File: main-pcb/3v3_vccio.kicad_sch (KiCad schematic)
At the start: 1 part, among them U1 XC7S100-1FGGA484C

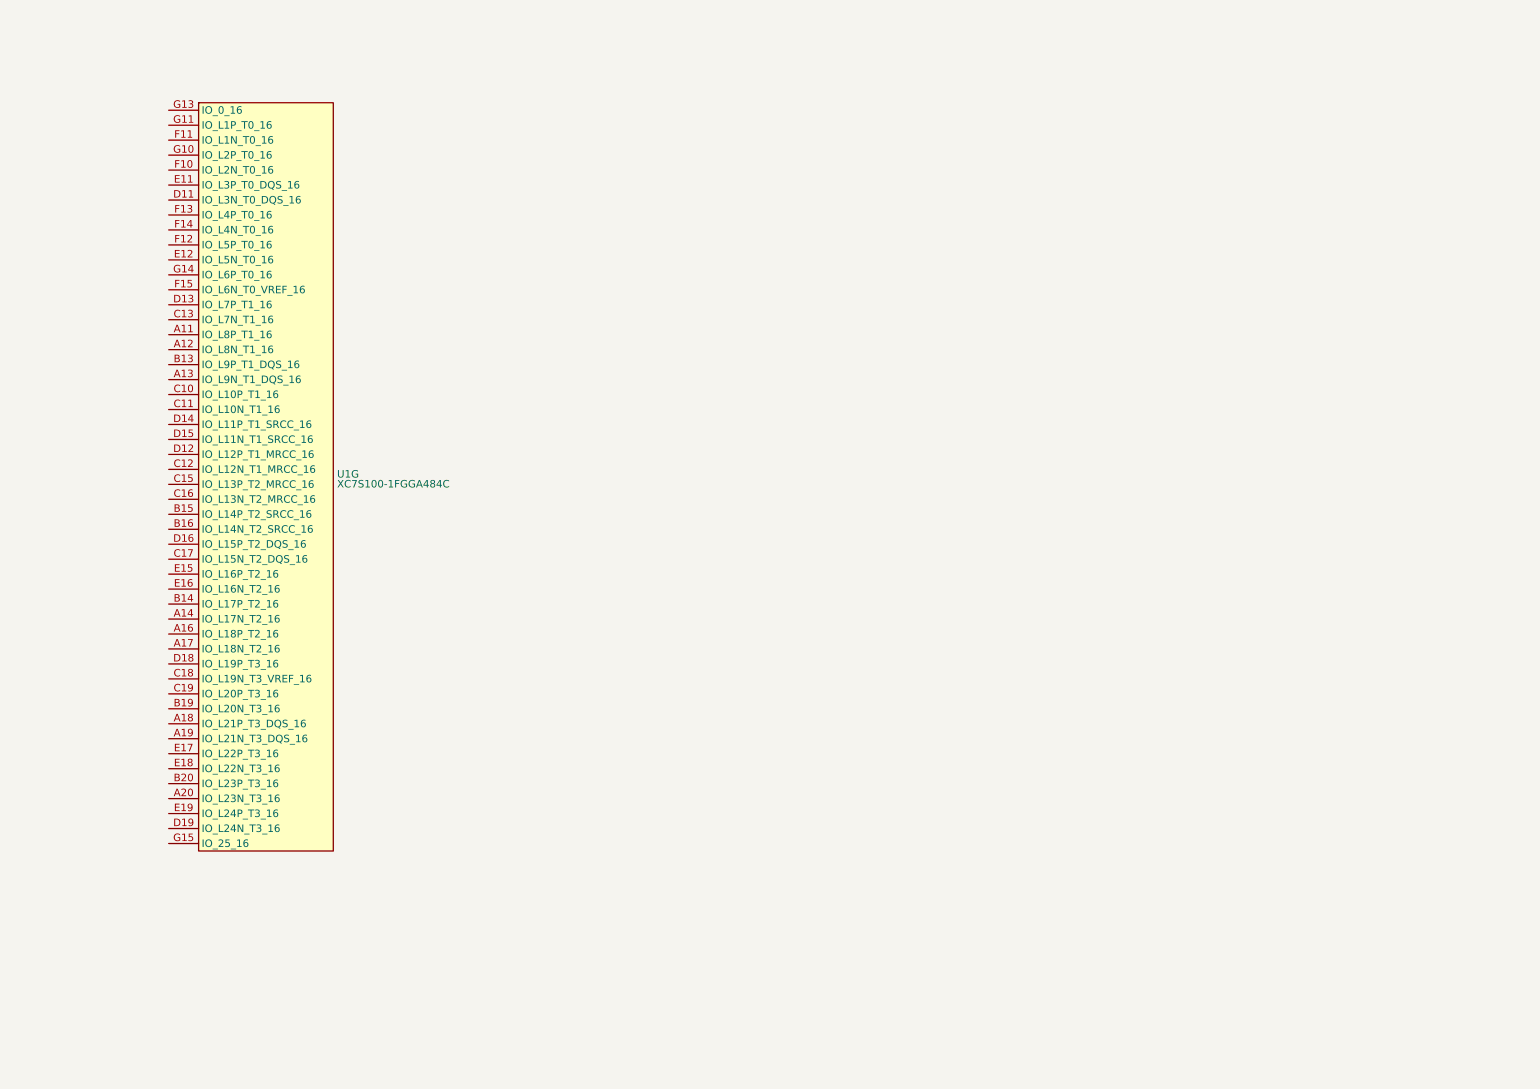
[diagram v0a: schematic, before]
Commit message: Initial design mostly done aside from USB connector, review, test points
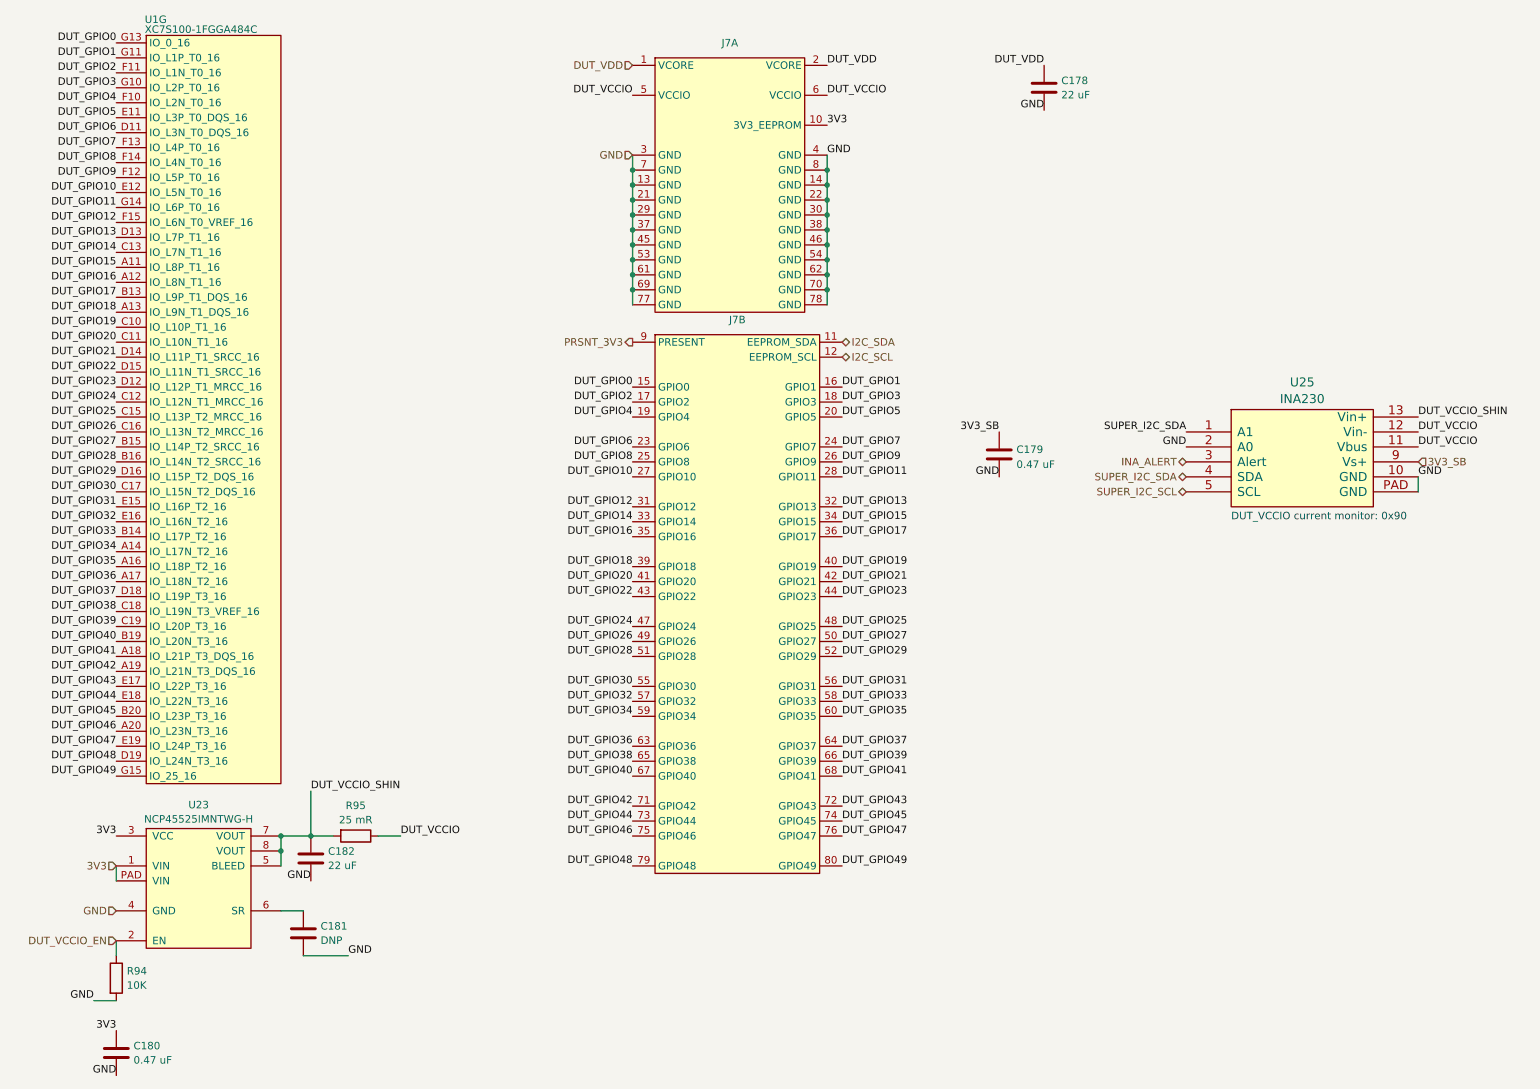
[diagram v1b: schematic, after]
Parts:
- added C178, C182: 22 uF, symbol device:C
- added C179: 0.47 uF, azonenberg_pcb:EIA_0402_CAP_NOSILK, symbol device:C
- added C180: 0.47 uF, symbol device:C
- added C181: DNP, symbol device:C
- added J7: ~, symbol special-azonenberg:CONN_DUMPTRUCK_HOST
- added R94: 10K, symbol device:R
- added R95: 25 mR, symbol passive-azonenberg:R_PWR
- added U23: NCP45525IMNTWG-H, symbol power-azonenberg:NCP45525
- added U25: INA230, azonenberg_pcb:QFN_16_0.5MM_3x3MM, symbol special-azonenberg:INA230
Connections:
- net DUT_GPIO15: now reaches U1.A11 (IO_L8P_T1_16)
- net DUT_GPIO15: now also J7.34 (GPIO15)
- net DUT_GPIO16: now reaches U1.A12 (IO_L8N_T1_16)
- net DUT_GPIO16: now also J7.35 (GPIO16)
- net DUT_GPIO18: now reaches U1.A13 (IO_L9N_T1_DQS_16)
- net DUT_GPIO18: now also J7.39 (GPIO18)
- net DUT_GPIO34: now reaches U1.A14 (IO_L17N_T2_16)
- net DUT_GPIO34: now also J7.59 (GPIO34)
- net DUT_GPIO35: now reaches U1.A16 (IO_L18P_T2_16)
- net DUT_GPIO35: now also J7.60 (GPIO35)
- net DUT_GPIO36: now reaches U1.A17 (IO_L18N_T2_16)
- net DUT_GPIO36: now also J7.63 (GPIO36)
- net DUT_GPIO41: now reaches U1.A18 (IO_L21P_T3_DQS_16)
- net DUT_GPIO41: now also J7.68 (GPIO41)
- net DUT_GPIO42: now reaches U1.A19 (IO_L21N_T3_DQS_16)
- net DUT_GPIO42: now also J7.71 (GPIO42)
- net DUT_GPIO46: now reaches U1.A20 (IO_L23N_T3_16)
- net DUT_GPIO46: now also J7.75 (GPIO46)
- net DUT_GPIO17: now reaches U1.B13 (IO_L9P_T1_DQS_16)
- net DUT_GPIO17: now also J7.36 (GPIO17)
- net DUT_GPIO33: now reaches U1.B14 (IO_L17P_T2_16)
- net DUT_GPIO33: now also J7.58 (GPIO33)
- net DUT_GPIO27: now reaches U1.B15 (IO_L14P_T2_SRCC_16)
- net DUT_GPIO27: now also J7.50 (GPIO27)
- net DUT_GPIO28: now reaches U1.B16 (IO_L14N_T2_SRCC_16)
- net DUT_GPIO28: now also J7.51 (GPIO28)
- net DUT_GPIO40: now reaches U1.B19 (IO_L20N_T3_16)
- net DUT_GPIO40: now also J7.67 (GPIO40)
- net DUT_GPIO45: now reaches U1.B20 (IO_L23P_T3_16)
- net DUT_GPIO45: now also J7.74 (GPIO45)
- net DUT_GPIO19: now reaches U1.C10 (IO_L10P_T1_16)
- net DUT_GPIO19: now also J7.40 (GPIO19)
- net DUT_GPIO20: now reaches U1.C11 (IO_L10N_T1_16)
- net DUT_GPIO20: now also J7.41 (GPIO20)
- net DUT_GPIO24: now reaches U1.C12 (IO_L12N_T1_MRCC_16)
- net DUT_GPIO24: now also J7.47 (GPIO24)
- net DUT_GPIO14: now reaches U1.C13 (IO_L7N_T1_16)
- net DUT_GPIO14: now also J7.33 (GPIO14)
- net DUT_GPIO25: now reaches U1.C15 (IO_L13P_T2_MRCC_16)
- net DUT_GPIO25: now also J7.48 (GPIO25)
- net DUT_GPIO26: now reaches U1.C16 (IO_L13N_T2_MRCC_16)
- net DUT_GPIO26: now also J7.49 (GPIO26)
- net DUT_GPIO30: now reaches U1.C17 (IO_L15N_T2_DQS_16)
- net DUT_GPIO30: now also J7.55 (GPIO30)
- net DUT_GPIO38: now reaches U1.C18 (IO_L19N_T3_VREF_16)
- net DUT_GPIO38: now also J7.65 (GPIO38)
- net DUT_GPIO39: now reaches U1.C19 (IO_L20P_T3_16)
- net DUT_GPIO39: now also J7.66 (GPIO39)
- net DUT_GPIO6: now reaches U1.D11 (IO_L3N_T0_DQS_16)
- net DUT_GPIO6: now also J7.23 (GPIO6)
- net DUT_GPIO23: now reaches U1.D12 (IO_L12P_T1_MRCC_16)
- net DUT_GPIO23: now also J7.44 (GPIO23)
- net DUT_GPIO13: now reaches U1.D13 (IO_L7P_T1_16)
- net DUT_GPIO13: now also J7.32 (GPIO13)
- net DUT_GPIO21: now reaches U1.D14 (IO_L11P_T1_SRCC_16)
- net DUT_GPIO21: now also J7.42 (GPIO21)
- net DUT_GPIO22: now reaches U1.D15 (IO_L11N_T1_SRCC_16)
- net DUT_GPIO22: now also J7.43 (GPIO22)
- net DUT_GPIO29: now reaches U1.D16 (IO_L15P_T2_DQS_16)
- net DUT_GPIO29: now also J7.52 (GPIO29)
- net DUT_GPIO37: now reaches U1.D18 (IO_L19P_T3_16)
- net DUT_GPIO37: now also J7.64 (GPIO37)
- net DUT_GPIO48: now reaches U1.D19 (IO_L24N_T3_16)
- net DUT_GPIO48: now also J7.79 (GPIO48)
- net DUT_GPIO5: now reaches U1.E11 (IO_L3P_T0_DQS_16)
- net DUT_GPIO5: now also J7.20 (GPIO5)
- net DUT_GPIO10: now reaches U1.E12 (IO_L5N_T0_16)
- net DUT_GPIO10: now also J7.27 (GPIO10)
- net DUT_GPIO31: now reaches U1.E15 (IO_L16P_T2_16)
- net DUT_GPIO31: now also J7.56 (GPIO31)
- net DUT_GPIO32: now reaches U1.E16 (IO_L16N_T2_16)
- net DUT_GPIO32: now also J7.57 (GPIO32)
- net DUT_GPIO43: now reaches U1.E17 (IO_L22P_T3_16)
- net DUT_GPIO43: now also J7.72 (GPIO43)
- net DUT_GPIO44: now reaches U1.E18 (IO_L22N_T3_16)
- net DUT_GPIO44: now also J7.73 (GPIO44)
- net DUT_GPIO47: now reaches U1.E19 (IO_L24P_T3_16)
- net DUT_GPIO47: now also J7.76 (GPIO47)
- net DUT_GPIO4: now reaches U1.F10 (IO_L2N_T0_16)
- net DUT_GPIO4: now also J7.19 (GPIO4)
- net DUT_GPIO2: now reaches U1.F11 (IO_L1N_T0_16)
- net DUT_GPIO2: now also J7.17 (GPIO2)
- net DUT_GPIO9: now reaches U1.F12 (IO_L5P_T0_16)
- net DUT_GPIO9: now also J7.26 (GPIO9)
- net DUT_GPIO7: now reaches U1.F13 (IO_L4P_T0_16)
- net DUT_GPIO7: now also J7.24 (GPIO7)
- net DUT_GPIO8: now reaches U1.F14 (IO_L4N_T0_16)
- net DUT_GPIO8: now also J7.25 (GPIO8)
- net DUT_GPIO12: now reaches U1.F15 (IO_L6N_T0_VREF_16)
- net DUT_GPIO12: now also J7.31 (GPIO12)
- net DUT_GPIO3: now reaches U1.G10 (IO_L2P_T0_16)
- net DUT_GPIO3: now also J7.18 (GPIO3)
- net DUT_GPIO1: now reaches U1.G11 (IO_L1P_T0_16)
- net DUT_GPIO1: now also J7.16 (GPIO1)
- net DUT_GPIO0: now reaches U1.G13 (IO_0_16)
- net DUT_GPIO0: now also J7.15 (GPIO0)
- net DUT_GPIO11: now reaches U1.G14 (IO_L6P_T0_16)
- net DUT_GPIO11: now also J7.28 (GPIO11)
- net DUT_GPIO49: now reaches U1.G15 (IO_25_16)
- net DUT_GPIO49: now also J7.80 (GPIO49)
- new net: C181.1, U23.6 (SR)
- new net 3V3: C180.1, J7.10 (3V3_EEPROM), U23.1 (VIN), U23.3 (VCC), U23.PAD (VIN)
- new net 3V3_SB: C179.1, U25.9 (Vs+)
- new net DUT_VCCIO: J7.5 (VCCIO), J7.6 (VCCIO), R95.1, U25.11 (Vbus), U25.12 (Vin-)
- new net DUT_VCCIO_EN: R94.1, U23.2 (EN)
- new net DUT_VCCIO_SHIN: C182.1, R95.2, U23.5 (BLEED), U23.7 (VOUT), U23.8 (VOUT), U25.13 (Vin+)
- new net DUT_VDD: C178.1, J7.1 (VCORE), J7.2 (VCORE)
- new net GND: C178.2, C179.2, C180.2, C181.2, C182.2, J7.13 (GND), J7.14 (GND), J7.21 (GND), J7.22 (GND), J7.29 (GND), J7.3 (GND), J7.30 (GND), J7.37 (GND), J7.38 (GND), J7.4 (GND), J7.45 (GND), J7.46 (GND), J7.53 (GND), J7.54 (GND), J7.61 (GND), J7.62 (GND), J7.69 (GND), J7.7 (GND), J7.70 (GND), J7.77 (GND), J7.78 (GND), J7.8 (GND), R94.2, U23.4 (GND), U25.10 (GND), U25.2 (A0), U25.PAD (GND)
- new net I2C_SCL: J7.12 (EEPROM_SCL)
- new net I2C_SDA: J7.11 (EEPROM_SDA)
- new net INA_ALERT: U25.3 (Alert)
- new net PRSNT_3V3: J7.9 (PRESENT)
- new net SUPER_I2C_SCL: U25.5 (SCL)
- new net SUPER_I2C_SDA: U25.1 (A1), U25.4 (SDA)
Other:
- note added: "DUT_VCCIO current monitor: 0x90"
- moved on the sheet: U1G

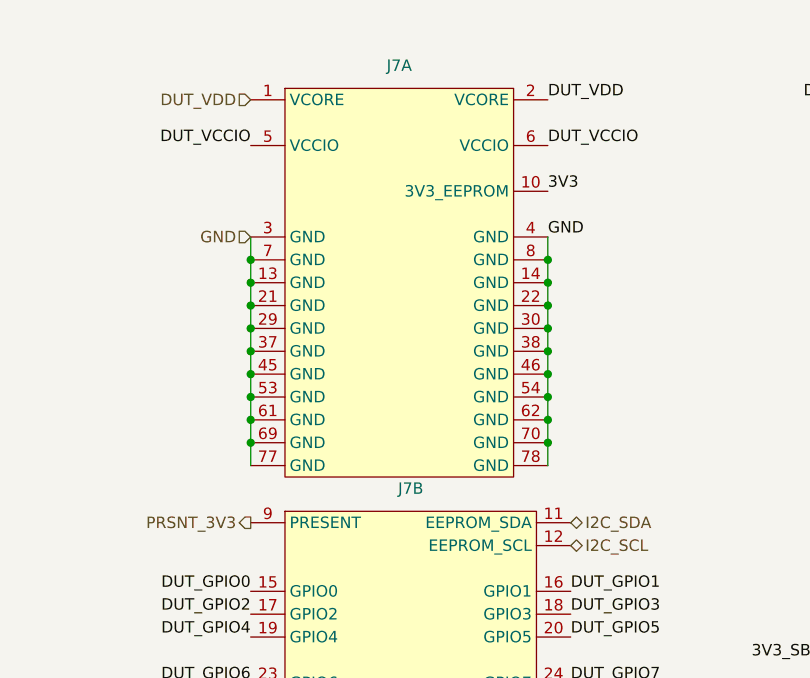
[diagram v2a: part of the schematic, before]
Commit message: More schematic tweaks and test points
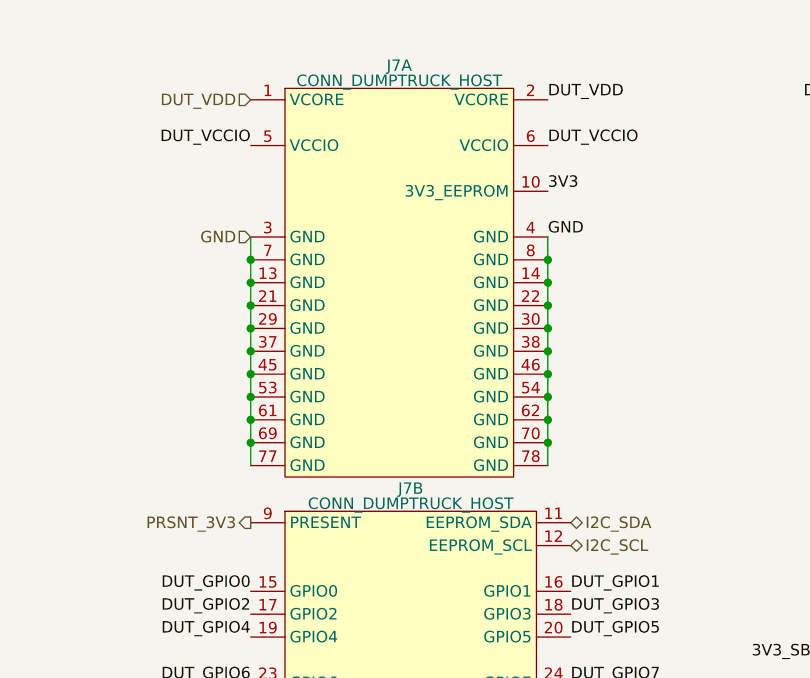
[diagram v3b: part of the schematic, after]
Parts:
- C180, C181: footprint (none) -> azonenberg_pcb:EIA_0402_CAP_NOSILK
- J7: value ~ -> CONN_DUMPTRUCK_HOST
- R94, R95: footprint (none) -> azonenberg_pcb:EIA_0402_RES_NOSILK
- U23: footprint (none) -> azonenberg_pcb:DFN_8_0.5MM_2x2MM
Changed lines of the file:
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@@
 			)
 		)
-		(property "Footprint" ""
+		(property "Footprint" "azonenberg_pcb:EIA_0402_CAP_NOSILK"
 			(at 79.7052 173.99 0)
 			(effects
@@
 			)
 		)
-		(property "Footprint" ""
+		(property "Footprint" "azonenberg_pcb:EIA_0402_CAP_NOSILK"
 			(at 47.9552 194.31 0)
 			(effects
@@
 			)
 		)
-		(property "Footprint" ""
+		(property "Footprint" "azonenberg_pcb:DFN_8_0.5MM_2x2MM"
 			(at 52.07 172.72 0)
 			(effects
@@
 			)
 		)
-		(property "Value" "~"
+		(property "Value" "CONN_DUMPTRUCK_HOST"
 			(at 151.13 20.7399 0)
 			(effects
@@
 			)
 		)
-		(property "Value" "~"
+		(property "Value" "CONN_DUMPTRUCK_HOST"
 			(at 152.4 67.7299 0)
 			(effects
@@
 			)
 		)
-		(property "Footprint" ""
+		(property "Footprint" "azonenberg_pcb:EIA_0402_RES_NOSILK"
 			(at 45.212 177.8 90)
 			(effects
@@
 			)
 		)
-		(property "Footprint" ""
+		(property "Footprint" "azonenberg_pcb:EIA_0402_RES_NOSILK"
 			(at 87.63 151.892 90)
 			(effects

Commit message: Added some RGB LEDs, changed a few voltage dividers to match what was in stock. Time for next round of review.
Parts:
- C178, C182: footprint (none) -> azonenberg_pcb:EIA_1210_CAP_NOSILK
- J7: footprint (none) -> azonenberg_pcb:CONN_SAMTEC_BTE-040-01-F-D-A-K
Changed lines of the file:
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@@
 	(title_block
 		(title "DUMPTRUCK flash dumper")
-		(date "2024-10-16")
+		(date "2024-10-17")
 		(rev "0.1")
 		(company "Antikernel Labs")
@@
 			)
 		)
-		(property "Footprint" ""
+		(property "Footprint" "azonenberg_pcb:EIA_1210_CAP_NOSILK"
 			(at 80.9752 161.29 0)
 			(effects
@@
 			)
 		)
-		(property "Footprint" ""
+		(property "Footprint" "azonenberg_pcb:CONN_SAMTEC_BTE-040-01-F-D-A-K"
 			(at 138.43 64.77 0)
 			(effects
@@
 			)
 		)
-		(property "Footprint" ""
+		(property "Footprint" "azonenberg_pcb:EIA_1210_CAP_NOSILK"
 			(at 205.4352 30.48 0)
 			(effects
@@
 			)
 		)
-		(property "Footprint" ""
+		(property "Footprint" "azonenberg_pcb:CONN_SAMTEC_BTE-040-01-F-D-A-K"
 			(at 138.43 160.02 0)
 			(effects
